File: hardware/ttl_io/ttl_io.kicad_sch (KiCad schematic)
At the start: 45 parts, among them J13 Conn_02x08_Counter_Clockwise, J14 Conn_02x08_Counter_Clockwise, SW2 SW_SPST, U14 74CBTLV3245, U15 74CBTLV3245, U16 74CBTLV3245, U17 74CBTLV3245, U18 74LVC1G04

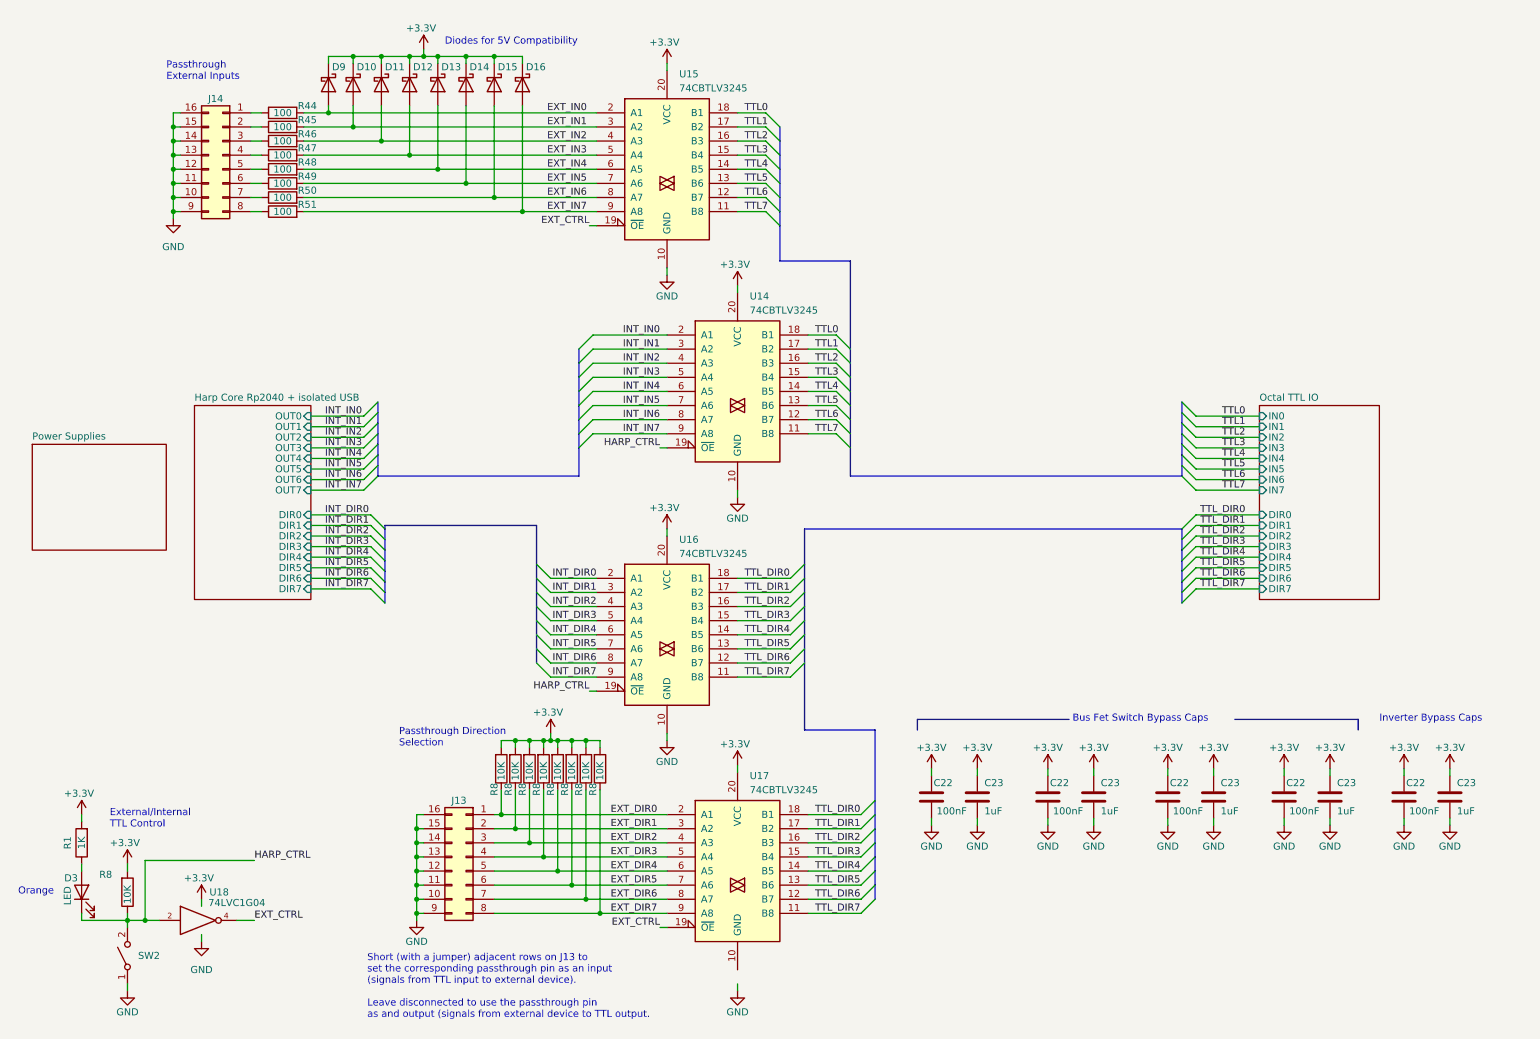
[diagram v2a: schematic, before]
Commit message: update passthrough level translator
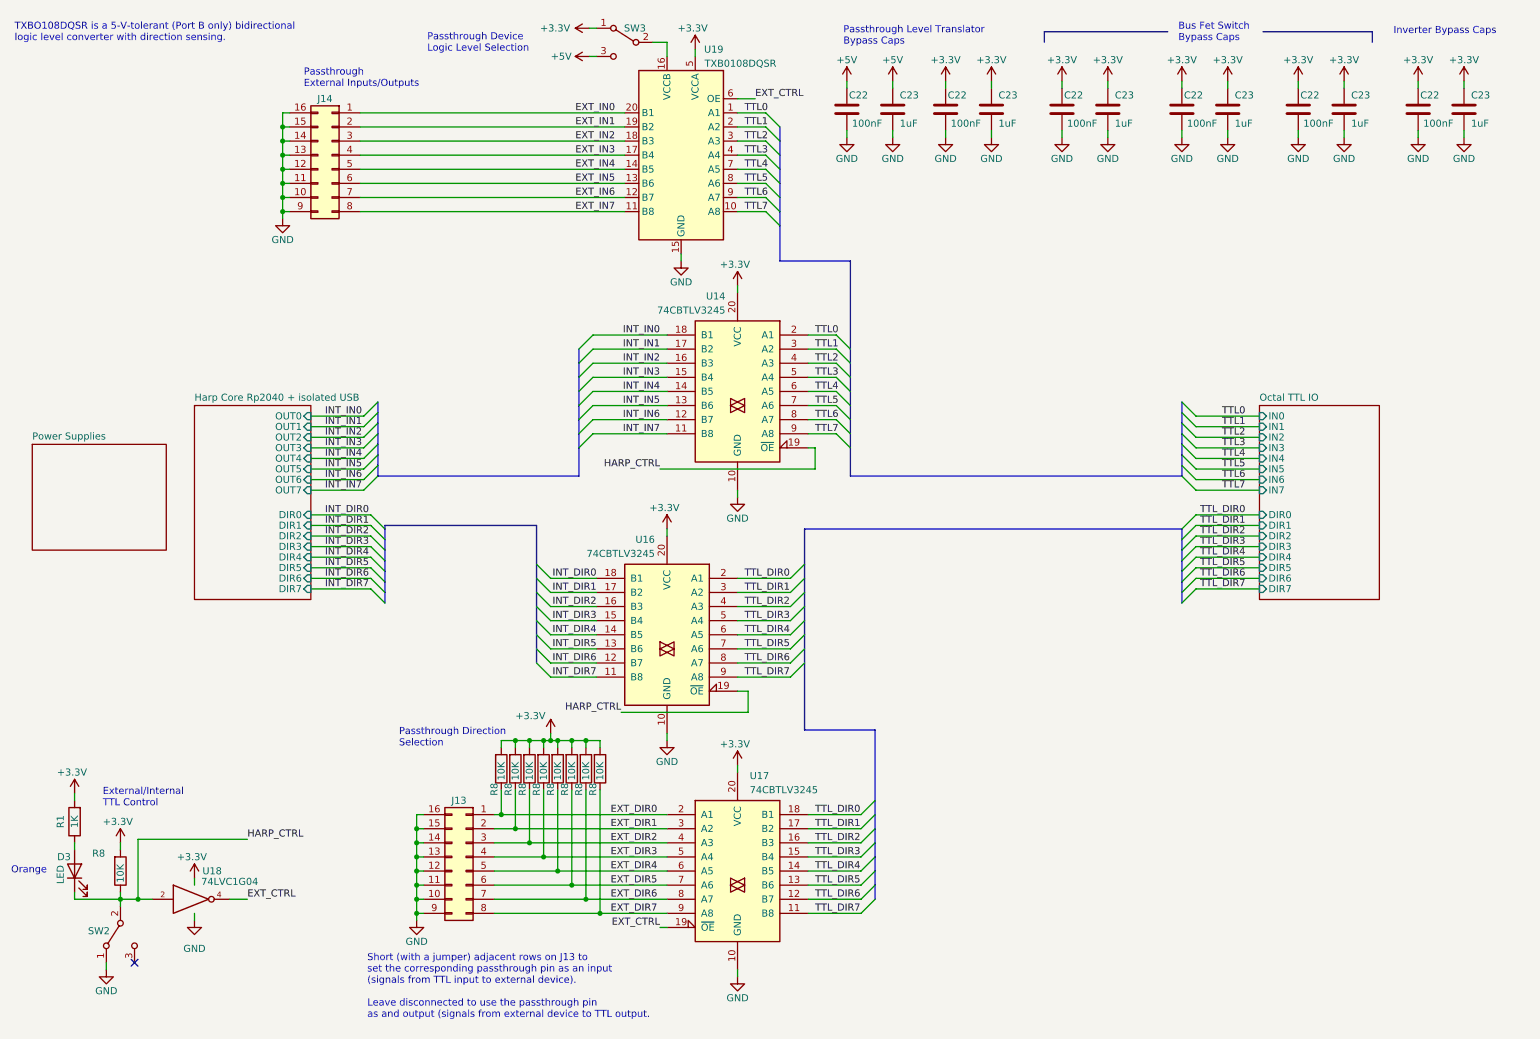
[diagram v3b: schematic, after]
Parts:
- removed D10, D11, D12, D13, D14, D15, D16, D9: D_Schottky, Diode_SMD:D_SOD-123, symbol Device:D_Schottky
- removed R44, R45, R46, R47, R48, R49, R50, R51: 100, symbol Device:R
- removed SW2: SW_SPST, symbol Switch:SW_SPST
- removed U15: 74CBTLV3245, Package_SO:TSSOP-20_4.4x6.5mm_P0.65mm, symbol kicad_component_library:74CBTLV3245
- added C22: 100nF, Capacitor_SMD:C_0402_1005Metric, symbol Device:C
- added C23: 1uF, Capacitor_SMD:C_0402_1005Metric, symbol Device:C
- added SW2, SW3: SW_SPDT, Button_Switch_SMD:SW_SPDT_CK-JS102011SAQN, symbol Switch:SW_SPDT
- added U19: TXB0108DQSR, Package_SON:USON-20_2x4mm_P0.4mm, symbol Logic_LevelTranslator:TXB0108DQSR
- J13, J14: footprint (none) -> Connector_PinHeader_2.54mm:PinHeader_2x08_P2.54mm_Vertical_SMD
- U14, U16, U17: Link (none) -> https://www.digikey.com/en/products/detail/nexperia-usa-inc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; Manufacturer (none) -> Nexperia USA Inc.; Manufacturer Number (none) -> 74CBTLV3245PW,118
- U18: footprint (none) -> Package_TO_SOT_SMD:SOT-23-5; Link (none) -> https://www.digikey.com/en/products/detail/texas-instrument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; Manufacturer (none) -> Texas Instruments; Manufacturer Number (none) -> SN74LVC1G04DBVR
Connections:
- net +3V3: now also SW3.1 (A), U19.5 (VCCA)
- net EXT_CTRL: now also U19.6 (OE)
- net EXT_IN0: now also J14.1 (Pin_1), U19.20 (B1)
- net EXT_IN1: now also J14.2 (Pin_2), U19.19 (B2)
- net EXT_IN2: now also J14.3 (Pin_3), U19.18 (B3)
- net EXT_IN3: now also J14.4 (Pin_4), U19.17 (B4)
- net EXT_IN4: now also J14.5 (Pin_5), U19.14 (B5)
- net EXT_IN5: now also J14.6 (Pin_6), U19.13 (B6)
- net EXT_IN6: now also J14.7 (Pin_7), U19.12 (B7)
- net EXT_IN7: now also J14.8 (Pin_8), U19.11 (B8)
- net GND: now also U17.10 (GND), C22.1, C23.2, SW2.1 (A), U19.15 (GND)
- net HARP_CTRL: now also SW2.2 (B)
- net INT_DIR0: now also U16.18 (B1); no longer U16.2 (A1)
- net INT_DIR1: now also U16.17 (B2); no longer U16.3 (A2)
- net INT_DIR2: now also U16.16 (B3); no longer U16.4 (A3)
- net INT_DIR3: now also U16.15 (B4); no longer U16.5 (A4)
- net INT_DIR4: now also U16.14 (B5); no longer U16.6 (A5)
- net INT_DIR5: now also U16.13 (B6); no longer U16.7 (A6)
- net INT_DIR6: now also U16.12 (B7); no longer U16.8 (A7)
- net INT_DIR7: now also U16.11 (B8); no longer U16.9 (A8)
- net INT_IN0: now also U14.18 (B1); no longer U14.2 (A1)
- net INT_IN1: now also U14.17 (B2); no longer U14.3 (A2)
- net INT_IN2: now also U14.16 (B3); no longer U14.4 (A3)
- net INT_IN3: now also U14.15 (B4); no longer U14.5 (A4)
- net INT_IN4: now also U14.14 (B5); no longer U14.6 (A5)
- net INT_IN5: now also U14.13 (B6); no longer U14.7 (A6)
- net INT_IN6: now also U14.12 (B7); no longer U14.8 (A7)
- net INT_IN7: now also U14.11 (B8); no longer U14.9 (A8)
- net TTL0: now also U14.2 (A1), U19.1 (A1); no longer U14.18 (B1)
- net TTL1: now also U14.3 (A2), U19.2 (A2); no longer U14.17 (B2)
- net TTL2: now also U14.4 (A3), U19.3 (A3); no longer U14.16 (B3)
- net TTL3: now also U14.5 (A4), U19.4 (A4); no longer U14.15 (B4)
- net TTL4: now also U14.6 (A5), U19.7 (A5); no longer U14.14 (B5)
- net TTL5: now also U14.7 (A6), U19.8 (A6); no longer U14.13 (B6)
- net TTL6: now also U14.8 (A7), U19.9 (A7); no longer U14.12 (B7)
- net TTL7: now also U14.9 (A8), U19.10 (A8); no longer U14.11 (B8)
- net TTL_DIR0: now also U16.2 (A1); no longer U16.18 (B1)
- net TTL_DIR1: now also U16.3 (A2); no longer U16.17 (B2)
- net TTL_DIR2: now also U16.4 (A3); no longer U16.16 (B3)
- net TTL_DIR3: now also U16.5 (A4); no longer U16.15 (B4)
- net TTL_DIR4: now also U16.6 (A5); no longer U16.14 (B5)
- net TTL_DIR5: now also U16.7 (A6); no longer U16.13 (B6)
- net TTL_DIR6: now also U16.8 (A7); no longer U16.12 (B7)
- net TTL_DIR7: now also U16.9 (A8); no longer U16.11 (B8)
- new net: SW3.2 (B), U19.16 (VCCB)
- new net +5V: C22.2, C23.1, SW3.3 (C)
- no-connect marks 0 -> 1
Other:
- note added: "Passthrough Device Logic Level Selection"
- note added: "Passthrough External Inputs/Outputs"
- note added: "Passthrough Level Translator Bypass Caps"
- note added: "TXBO108DQSR is a 5-V-tolerant (Port B only) bidirectional logic level converter with direction sensing."
- note removed: "Diodes for 5V Compatibility"
- note removed: "Passthrough External Inputs"
- moved on the sheet: C22, C23, D3, J14, R1, R8, U18

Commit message: update layout
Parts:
- removed D3: LED, LED_SMD:LED_0603_1608Metric, symbol Device:LED
- removed R1: 1K, Resistor_SMD:R_0402_1005Metric, symbol Device:R
- removed R8: 10K, Resistor_SMD:R_0402_1005Metric, symbol Device:R
- removed SW2: SW_SPDT, Button_Switch_SMD:SW_SPDT_CK-JS102011SAQN, symbol Switch:SW_SPDT
- removed U18: 74LVC1G04, Package_TO_SOT_SMD:SOT-23-5, symbol 74xGxx:74LVC1G04
- J13, J14: footprint Connector_PinHeader_2.54mm:PinHeader_2x08_P2.54mm_Vertical_SMD -> kicad_component_library:PinHeader_2x08_P2.54mm_Horizontal_SMD
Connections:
- net EXT_CTRL: no longer U17.19 (~{OE})
- net EXT_DIR0: now also J13.16 (Pin_16); no longer J13.1 (Pin_1)
- net EXT_DIR1: now also J13.15 (Pin_15); no longer J13.2 (Pin_2)
- net EXT_DIR2: now also J13.14 (Pin_14); no longer J13.3 (Pin_3)
- net EXT_DIR3: now also J13.13 (Pin_13); no longer J13.4 (Pin_4)
- net EXT_DIR4: now also J13.12 (Pin_12); no longer J13.5 (Pin_5)
- net EXT_DIR5: now also J13.11 (Pin_11); no longer J13.6 (Pin_6)
- net EXT_DIR6: now also J13.10 (Pin_10); no longer J13.7 (Pin_7)
- net EXT_DIR7: now also J13.9 (Pin_9); no longer J13.8 (Pin_8)
- net EXT_IN0: now also J14.16 (Pin_16), U19.11 (B8); no longer J14.1 (Pin_1), U19.20 (B1)
- net EXT_IN1: now also J14.15 (Pin_15), U19.12 (B7); no longer J14.2 (Pin_2), U19.19 (B2)
- net EXT_IN2: now also J14.14 (Pin_14), U19.13 (B6); no longer J14.3 (Pin_3), U19.18 (B3)
- net EXT_IN3: now also J14.13 (Pin_13), U19.14 (B5); no longer J14.4 (Pin_4), U19.17 (B4)
- net EXT_IN4: now also J14.12 (Pin_12), U19.17 (B4); no longer J14.5 (Pin_5), U19.14 (B5)
- net EXT_IN5: now also J14.11 (Pin_11), U19.18 (B3); no longer J14.6 (Pin_6), U19.13 (B6)
- net EXT_IN6: now also J14.10 (Pin_10), U19.19 (B2); no longer J14.7 (Pin_7), U19.12 (B7)
- net EXT_IN7: now also J14.9 (Pin_9), U19.20 (B1); no longer J14.8 (Pin_8), U19.11 (B8)
- net GND: now also J13.1 (Pin_1), J13.2 (Pin_2), J13.3 (Pin_3), J13.4 (Pin_4), J13.5 (Pin_5), J13.6 (Pin_6), J13.7 (Pin_7), J13.8 (Pin_8), J14.1 (Pin_1), J14.2 (Pin_2), J14.3 (Pin_3), J14.4 (Pin_4), J14.5 (Pin_5), J14.6 (Pin_6), J14.7 (Pin_7), J14.8 (Pin_8); no longer J13.10 (Pin_10), J13.11 (Pin_11), J13.12 (Pin_12), J13.13 (Pin_13), J13.14 (Pin_14), J13.15 (Pin_15), J13.16 (Pin_16), J13.9 (Pin_9), J14.10 (Pin_10), J14.11 (Pin_11), J14.12 (Pin_12), J14.13 (Pin_13), J14.14 (Pin_14), J14.15 (Pin_15), J14.16 (Pin_16), J14.9 (Pin_9)
- net TTL0: now also U19.10 (A8); no longer U19.1 (A1)
- net TTL1: now also U19.9 (A7); no longer U19.2 (A2)
- net TTL2: now also U19.8 (A6); no longer U19.3 (A3)
- net TTL3: now also U19.7 (A5); no longer U19.4 (A4)
- net TTL4: now also U19.4 (A4); no longer U19.7 (A5)
- net TTL5: now also U19.3 (A3); no longer U19.8 (A6)
- net TTL6: now also U19.2 (A2); no longer U19.9 (A7)
- net TTL7: now also U19.1 (A1); no longer U19.10 (A8)
- net HARP_CTRL renamed ~{HARP_CTRL}
- new net ~{EXT_CTRL}: U17.19 (~{OE})
- no-connect marks 1 -> 0
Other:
- added sheet Bus Selection (bus_selection.kicad_sch)
- note removed: "External/Internal TTL Control"
- note removed: "Orange"
- moved on the sheet: C22, C23, J13, J14, R8, SW3, U14, U16, U17, U19

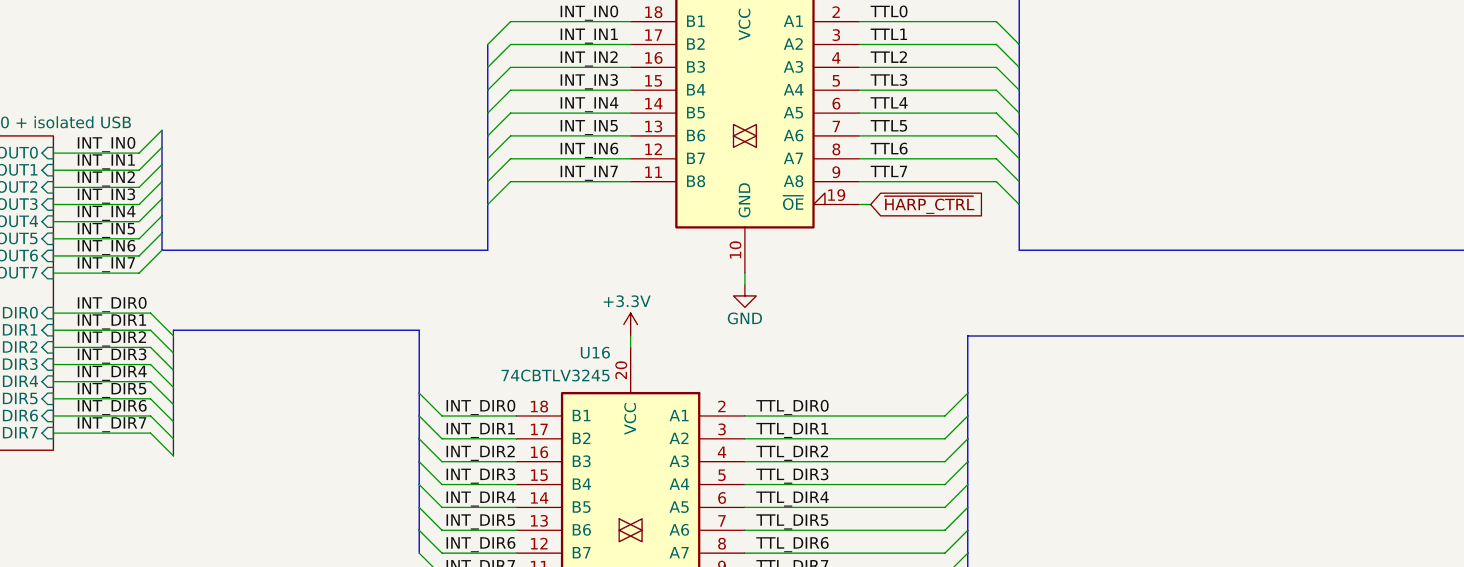
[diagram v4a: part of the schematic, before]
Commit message: update power supply schematic/board
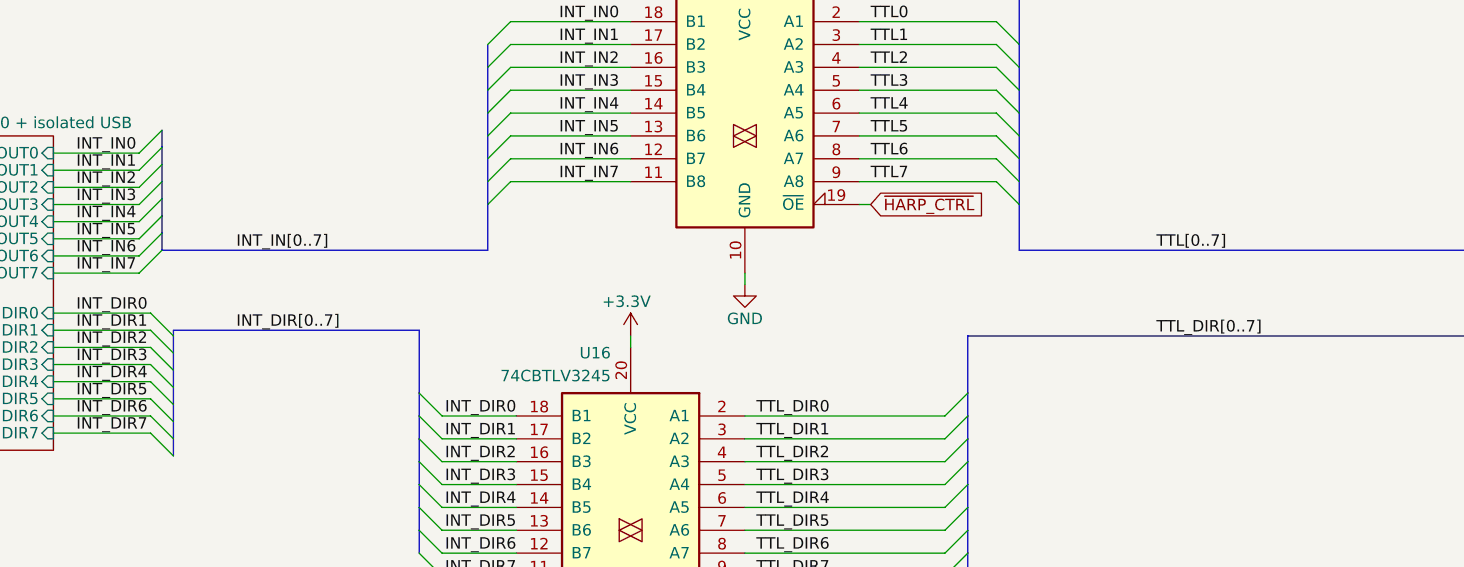
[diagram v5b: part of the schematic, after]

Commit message: annotate bus logic on schematic
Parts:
- added R8: 10K, Resistor_SMD:R_0402_1005Metric, symbol Device:R
- U19: value TXB0108DQSR -> TXB0108; footprint Package_SON:USON-20_2x4mm_P0.4mm -> Package_SO:TSSOP-20_4.4x6.5mm_P0.65mm; Link https://www.digikey.com/en/products/detail/texas-instruments/TXB0108DQSR/2260592?s=N4IgTCBcDaICoA0BCAGAjCgHAEQIoGUAlEAXQF8g -> https://www.digikey.com/en/products/detail/texas-instruments/TXB0108PWR/1305699; Manufacturer Number TXB0108DQSR -> TXB0108PWR
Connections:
- net GND: now also R8.1
- net at SW3.2 (B), U19.16 (VCCB): now also R8.2
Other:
- sheet Bus Selection ports: added BUS_STATE; removed none
- sheet Harp Core Rp2040 + isolated USB ports: added BUS_STATE; removed none
- note added: "Bus Selection Truth Table"
- note added: "Input: 0V | 3.3V D9 LED: on | off U19: enabled | disabled U17: enabled | disabled U14: disabled | enabled U16: disabled | enabled"
- moved on the sheet: SW3

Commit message: update pcb
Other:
- moved on the sheet: C22, C23, J13, J14, R8, SW3, U14, U16, U17, U19

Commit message: update pcb
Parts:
- removed C22: 100nF, Capacitor_SMD:C_0402_1005Metric, symbol Device:C
- removed C23: 1uF, Capacitor_SMD:C_0402_1005Metric, symbol Device:C
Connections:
- net +5V: no longer C22.2
- net at R8.2, SW3.2 (B), U19.16 (VCCB): now also C22.2
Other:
- note added: "Bypass"
- note added: "Input: 0V | 3.3V D9 LED: on | off BUS_STATE: 0V | 3.3V Mode: EXT | INT U19: enabled | disabled U17: enabled | disabled U14: disabled | enabled U16: disabled | enabled"
- note removed: "Input: 0V | 3.3V D9 LED: on | off U19: enabled | disabled U17: enabled | disabled U14: disabled | enabled U16: disabled | enabled"
- note removed: "Inverter Bypass Caps"
- moved on the sheet: C22, C23
